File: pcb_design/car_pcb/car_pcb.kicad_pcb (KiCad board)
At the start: 2 copper layers, 158 x 115 mm, 28 parts, among them J1 PICO_R, J10 CMD_UART, J11 +5V, J12 PICO_L, J14 PWR_OUTPUT, J16 NRF24L01, J18 GND, J19 +3.3V, J2 PWR_INPUT, J20 GND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

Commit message: update pcbs
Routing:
- net GND: track 515.9 -> 525.2 mm
- net Net-(J7-Pin_1): track 164.6 -> 169.8 mm
- net Net-(J5-Pin_1): track 145.2 -> 149.0 mm
- net Net-(A1-GP27): track 200.3 -> 204.0 mm
- net Net-(A1-GP17): track 57.7 -> 60.9 mm
- net Net-(J7-Pin_2): track 158.0 -> 160.7 mm
- net +3.3V: track 303.4 -> 306.0 mm
- net Net-(A1-GP13): track 121.6 -> 124.1 mm
- net Net-(A1-GP1): track 164.5 -> 166.4 mm
- net Net-(A1-GP2): track 120.5 -> 121.9 mm
- net Net-(A1-GP3): track 118.5 -> 119.8 mm
- net Net-(A1-GP26): track 191.9 -> 193.0 mm
- net Net-(J5-Pin_2): track 139.6 -> 140.7 mm
- net Net-(A1-GP4): track 176.0 -> 177.0 mm
- net Net-(A1-GP14): track 164.2 -> 165.2 mm
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- added copper zone on B.Cu, net GND
- added copper zone on F.Cu, net GND
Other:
- board text added: "+12V"
- board text added: "+3.3V"
- board text added: "+5V"
- board text added: "GND"
- board text added: "Joystick-X"
- board text added: "Joystick-Y"
- board text added: "RX"
- board text added: "SIG"
- board text added: "TR_24_RC_AUTO_rev_1.1"
- board text added: "TX"
- board text added: "X"
- board text added: "Y"

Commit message: update pcbs
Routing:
- net Net-(A1-RUN): track 69.5 -> 116.3 mm
- net Net-(A1-GP22): track 68.2 -> 111.3 mm, vias 1 -> 0
- net Net-(A1-GP21): track 80.1 -> 121.2 mm, vias 2 -> 1
- net Net-(A1-GP13): track 124.1 -> 87.1 mm, vias 1 -> 0
- net Net-(A1-GP20): track 82.2 -> 104.1 mm
- net Net-(A1-ADC_VREF): track 84.4 -> 106.2 mm, vias 0 -> 1
- net Net-(A1-GP14): track 165.2 -> 147.9 mm
- net Net-(A1-GP4): track 177.0 -> 194.3 mm
- net +3.3V: track 306.0 -> 288.9 mm, vias 0 -> 1
- net Net-(A1-GP5): track 168.4 -> 184.7 mm
- net Net-(A1-GP28): track 90.6 -> 106.8 mm, vias 0 -> 1
- net Net-(A1-AGND): track 128.0 -> 143.9 mm, vias 2 -> 1
- net Net-(J7-Pin_1): track 169.8 -> 185.1 mm, vias 0 -> 1
- net Net-(J7-Pin_2): track 160.7 -> 175.9 mm
- net Net-(A1-3V3_EN): track 92.2 -> 105.4 mm, vias 0 -> 1
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
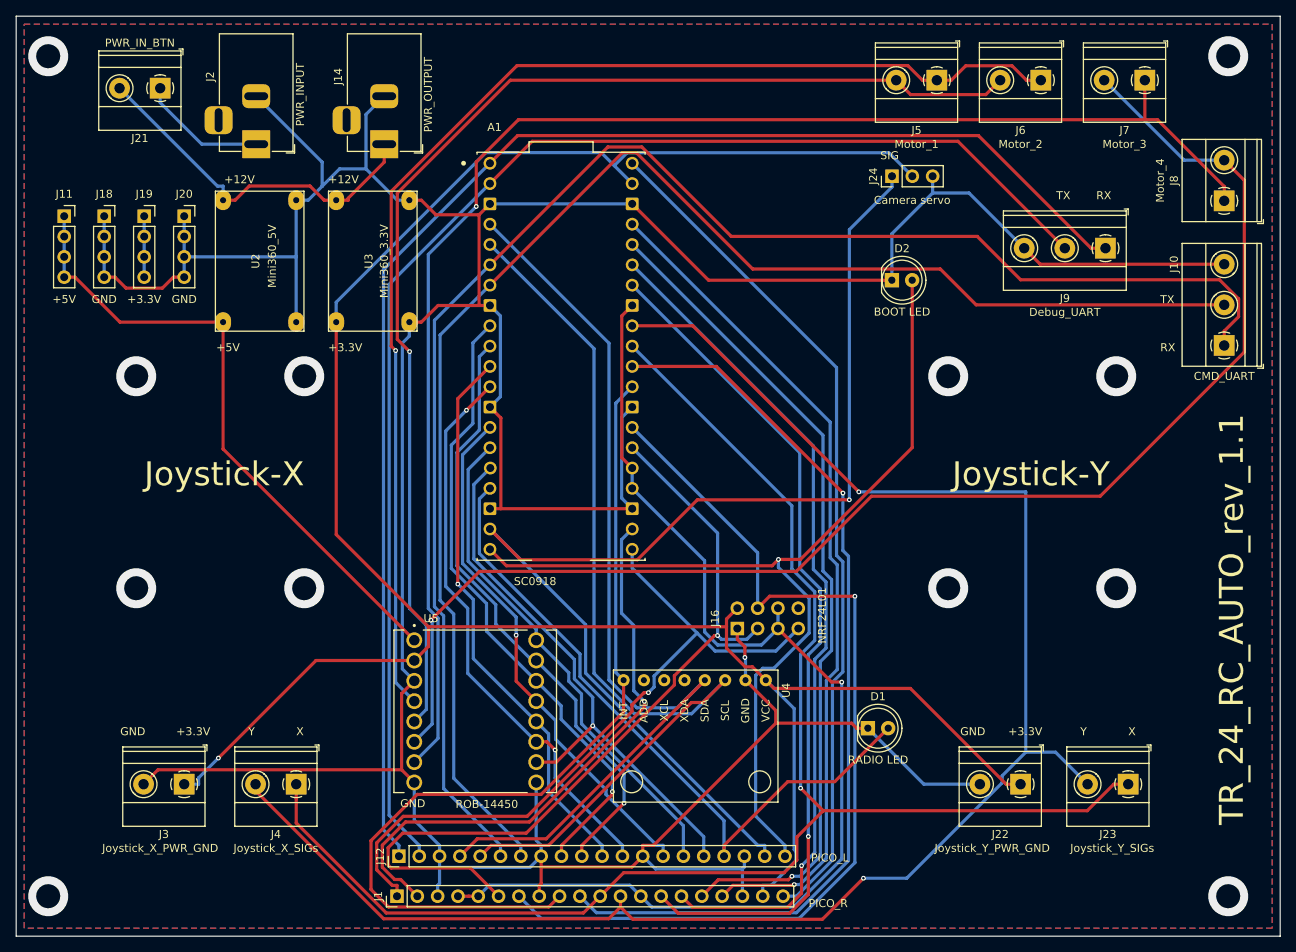
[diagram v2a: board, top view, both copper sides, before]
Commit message: fix issue with mistakes in rev 1.1. Now rev 1.2 is ready
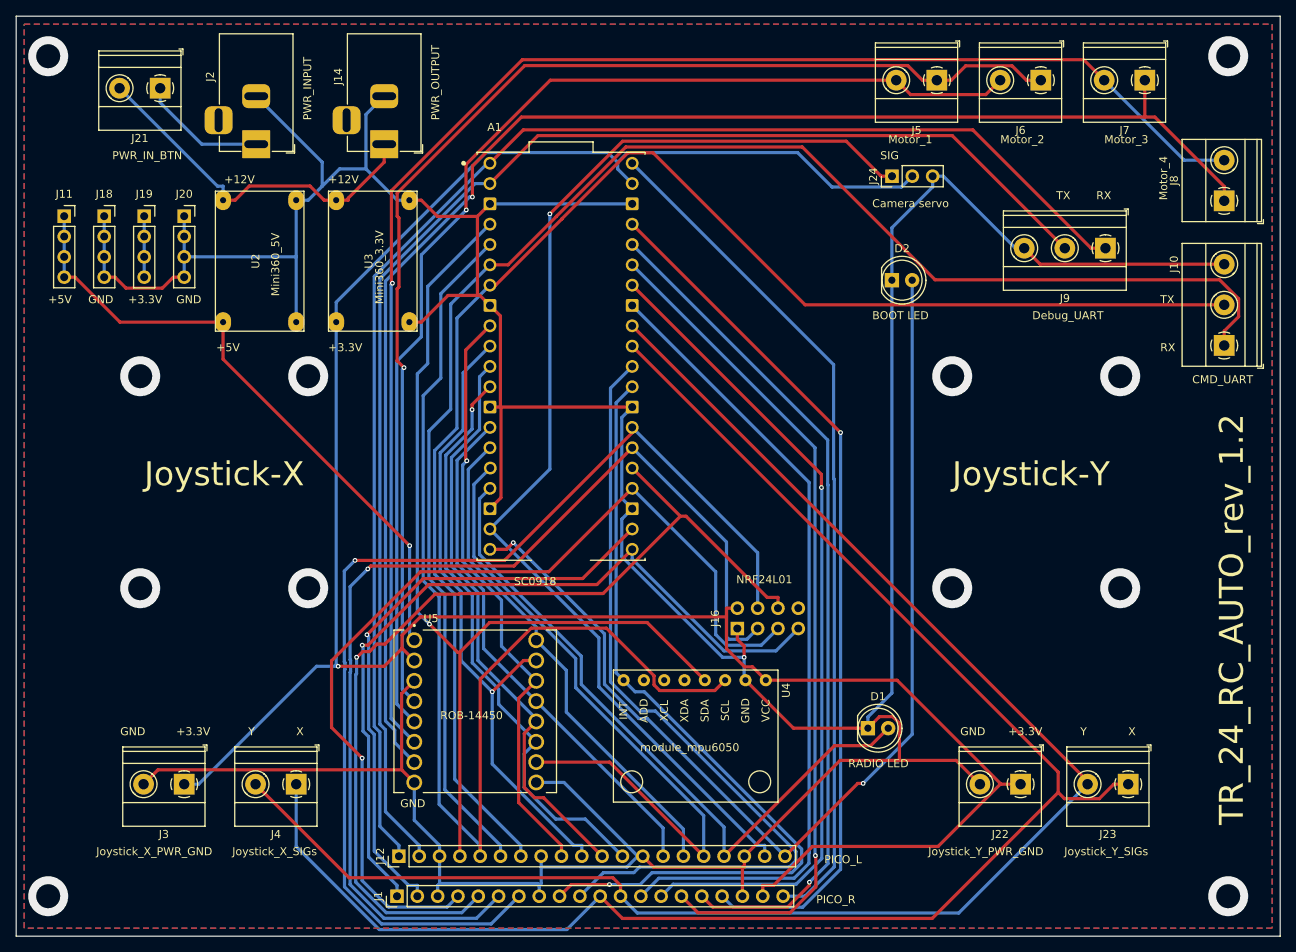
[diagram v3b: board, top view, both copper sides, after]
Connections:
- A1 pad 24: Net-(A1-AGND) -> Net-(A1-GP18)
- A1 pad 25: Net-(A1-AGND) -> Net-(A1-GP19)
- J1 pad 4: Net-(A1-AGND) -> Net-(A1-GP18)
- J1 pad 5: Net-(A1-AGND) -> Net-(A1-GP19)
- J16 pad 5: Net-(A1-AGND) -> Net-(A1-GP18)
- J16 pad 6: Net-(A1-AGND) -> Net-(A1-GP19)
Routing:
- net Net-(A1-GP18): track 0.00 -> 121.3 mm, vias 0 -> 1
- net Net-(A1-GP19): track 0.00 -> 120.0 mm, vias 0 -> 1
- net Net-(A1-AGND): track 143.9 -> 101.6 mm, vias 1 -> 0
- net Net-(A1-GP20): track 104.1 -> 134.3 mm
- net Net-(A1-GP3): track 119.0 -> 142.7 mm
- net Net-(A1-GP12): track 70.2 -> 87.1 mm, vias 1 -> 0
- net Net-(A1-GP21): track 121.2 -> 137.6 mm
- net Net-(A1-GP27): track 215.2 -> 199.0 mm, vias 2 -> 0
- net Net-(A1-RUN): track 116.3 -> 102.5 mm, vias 1 -> 0
- net Net-(A1-GP26): track 191.3 -> 204.4 mm, vias 1 -> 0
- net Net-(A1-GP15): track 124.5 -> 136.1 mm, vias 1 -> 2
- net GND: track 534.0 -> 545.5 mm
- net Net-(A1-GP16): track 88.9 -> 99.8 mm
- net Net-(J7-Pin_2): track 175.9 -> 186.3 mm
- net +3.3V: track 288.9 -> 298.2 mm
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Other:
- board text added: "BOOT LED"
- board text added: "CMD_UART"
- board text added: "Camera servo"
- board text added: "Debug_UART"
- board text added: "Joystick_X_PWR_GND"
- board text added: "Joystick_X_SIGs"
- board text added: "Joystick_Y_PWR_GND"
- board text added: "Joystick_Y_SIGs"
- board text added: "Mini360_3.3V"
- board text added: "Mini360_5V"
- board text added: "Motor_1"
- board text added: "Motor_2"
- board text added: "Motor_3"
- board text added: "Motor_4"
- board text added: "NRF24L01"
- board text added: "PICO_L"
- board text added: "PICO_R"
- board text added: "PWR_INPUT"
- board text added: "PWR_IN_BTN"
- board text added: "PWR_OUTPUT"
- board text added: "RADIO LED"
- board text added: "ROB-14450"
- board text added: "TR_24_RC_AUTO_rev_1.2"
- board text added: "module_mpu6050"
- board text removed: "TR_24_RC_AUTO_rev_1.1"
